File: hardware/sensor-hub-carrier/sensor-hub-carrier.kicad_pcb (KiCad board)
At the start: 2 copper layers, 39.6 x 73.2 mm, 6 parts, among them U1 ESP32-S3-DEVKITC-1-N8R2

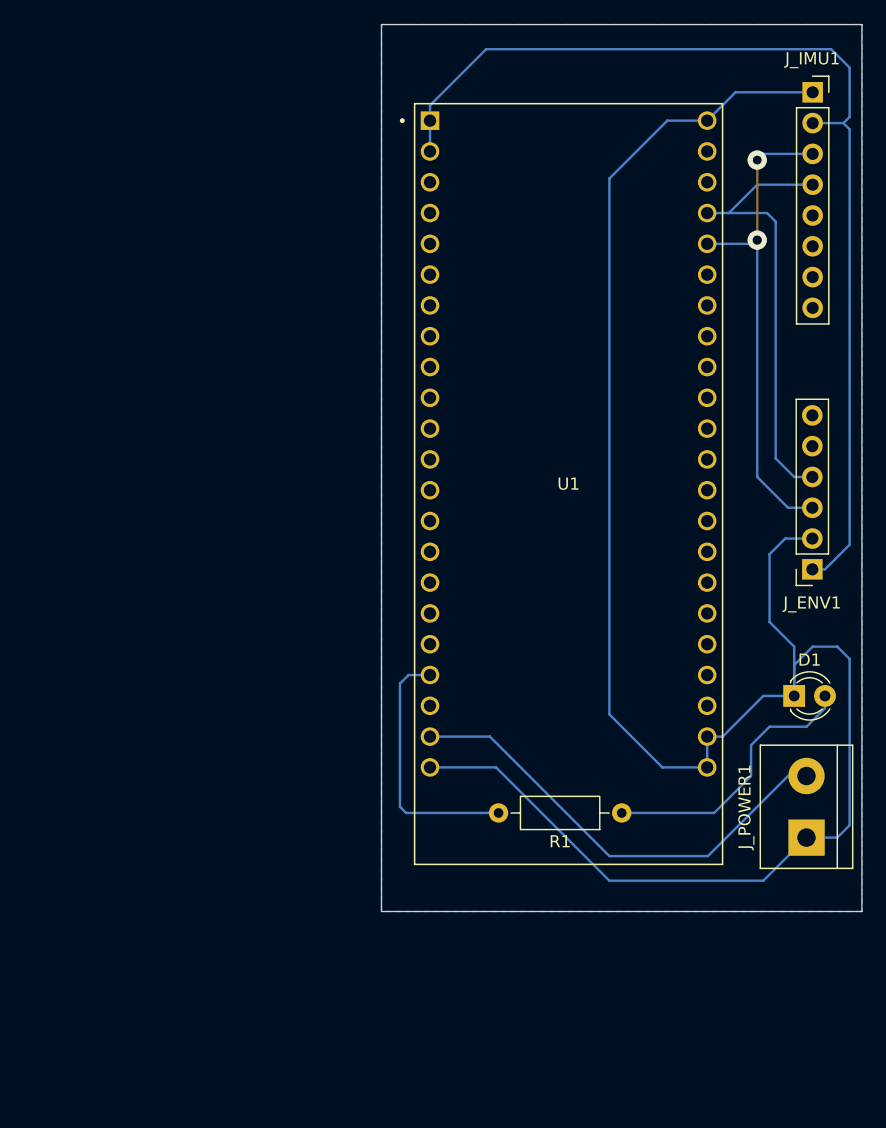
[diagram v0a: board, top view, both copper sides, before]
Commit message: docs: Release Hardware v1.1 (Relay Driver + Expansion Ports)
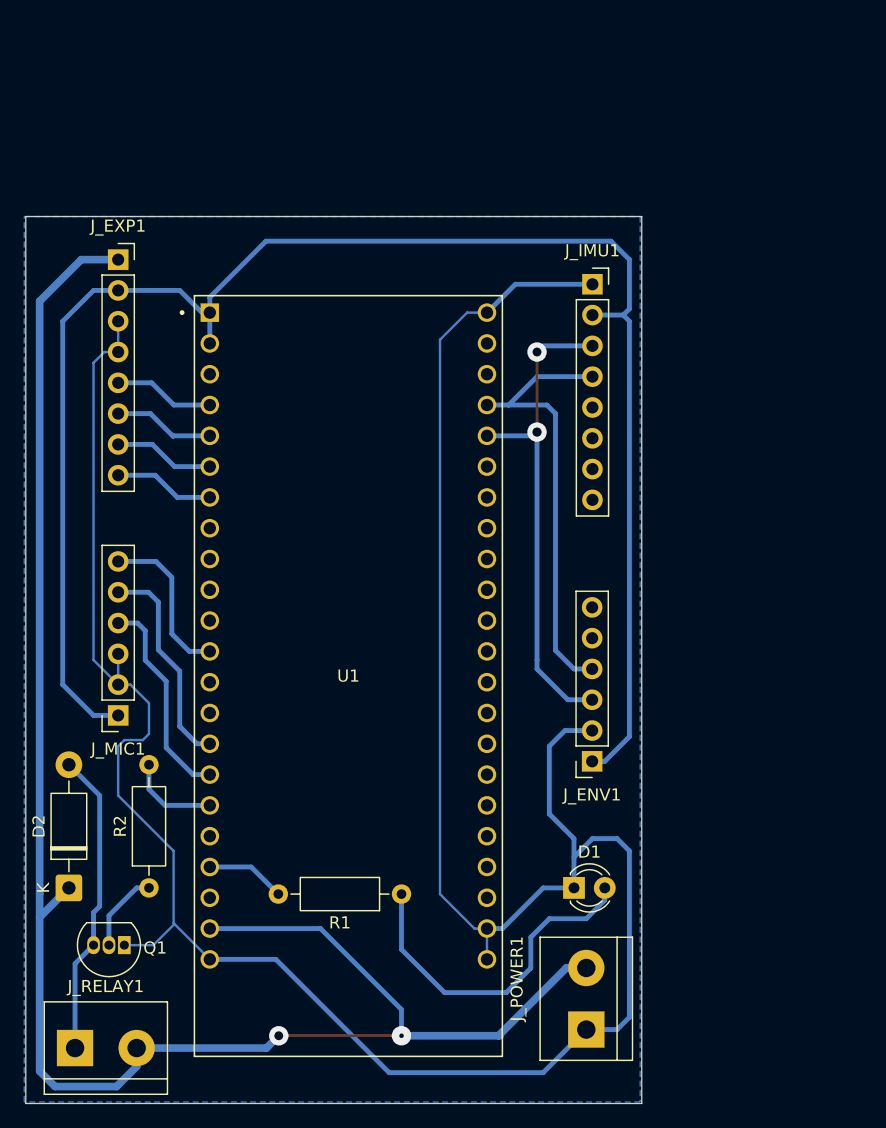
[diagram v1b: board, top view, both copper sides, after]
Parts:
- added D2: 1N4007, Diode_THT:D_DO-41_SOD81_P10.16mm_Horizontal, F.Cu at (25.5, 172.8)
- added J_EXP1: EXP, Connector_PinSocket_2.54mm:PinSocket_1x08_P2.54mm_Vertical, F.Cu at (29.6, 121.0)
- added J_MIC1: INMP441, Connector_PinSocket_2.54mm:PinSocket_1x06_P2.54mm_Vertical, F.Cu at (29.6, 158.6)
- added J_RELAY1: 5V, TerminalBlock:TerminalBlock_bornier-2_P5.08mm, F.Cu at (26.0, 186.0)
- added Q1: 2N3904, Package_TO_SOT_THT:TO-92_Inline, F.Cu at (30.1, 177.5)
- added R2: 1K, Resistor_THT:R_Axial_DIN0207_L6.3mm_D2.5mm_P10.16mm_Horizontal, F.Cu at (32.1, 172.8)
- J_POWER1: value Screw_Terminal_01x02 -> +5V
- U1: value ESP32-S3-DEVKITC-1-N8R2 -> ESP32-S3-DEVKITC-1-N16R8
- moved J_ENV1 24.1 mm to (68.7, 162.4)
- moved J_IMU1 24.1 mm to (68.7, 123.0)
- moved J_POWER1 24.1 mm to (68.2, 184.5)
- moved U1 24.1 mm to (48.6, 155.3)
- moved D1 24.1 mm to (67.2, 172.8)
- moved R1 19.4 mm to (53.0, 173.3)
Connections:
- U1 pad J1_12: unconnected-(U1-GPIO8-PadJ1_12) -> /SD
- U1 pad J1_15: unconnected-(U1-GPIO9-PadJ1_15) -> /WS
- U1 pad J1_16: unconnected-(U1-GPIO10-PadJ1_16) -> /SCK
- U1 pad J1_17: unconnected-(U1-GPIO11-PadJ1_17) -> /GPIO11
- U1 pad J1_4: unconnected-(U1-GPIO4-PadJ1_4) -> /GPIO4
- U1 pad J1_5: unconnected-(U1-GPIO5-PadJ1_5) -> /GPIO5
- U1 pad J1_6: unconnected-(U1-GPIO6-PadJ1_6) -> /GPIO6
- U1 pad J1_7: unconnected-(U1-GPIO7-PadJ1_7) -> /GPIO7
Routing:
- net VCC: track 37.9 -> 148.0 mm, vias 0 -> 2
- net GND: track 163.7 -> 224.3 mm
- net 3V3: track 87.2 -> 136.7 mm
- net Net-(D2-A): track 0.00 -> 25.3 mm
- net /WS: track 0.00 -> 17.7 mm
- net /SCK: track 0.00 -> 17.4 mm
- net Net-(U1-GPIO13): track 21.3 -> 6.58 mm
- net /SD: track 0.00 -> 13.4 mm
- net /GPIO5: track 0.00 -> 8.34 mm
- net /GPIO7: track 0.00 -> 8.32 mm
- net /GPIO6: track 0.00 -> 8.32 mm
- net /GPIO4: track 0.00 -> 8.32 mm
- net /GPIO11: track 0.00 -> 7.60 mm
- net Net-(Q1-B): track 0.00 -> 6.68 mm
- net Net-(D1-A): track 22.8 -> 28.5 mm
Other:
- board size 39.6 x 73.2 mm -> 50.8 x 73.2 mm
